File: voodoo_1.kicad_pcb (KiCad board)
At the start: 2 copper layers, 70 x 50 mm, 37 parts, among them Q1 2N2222, Q2 2N2222, U1 LM308

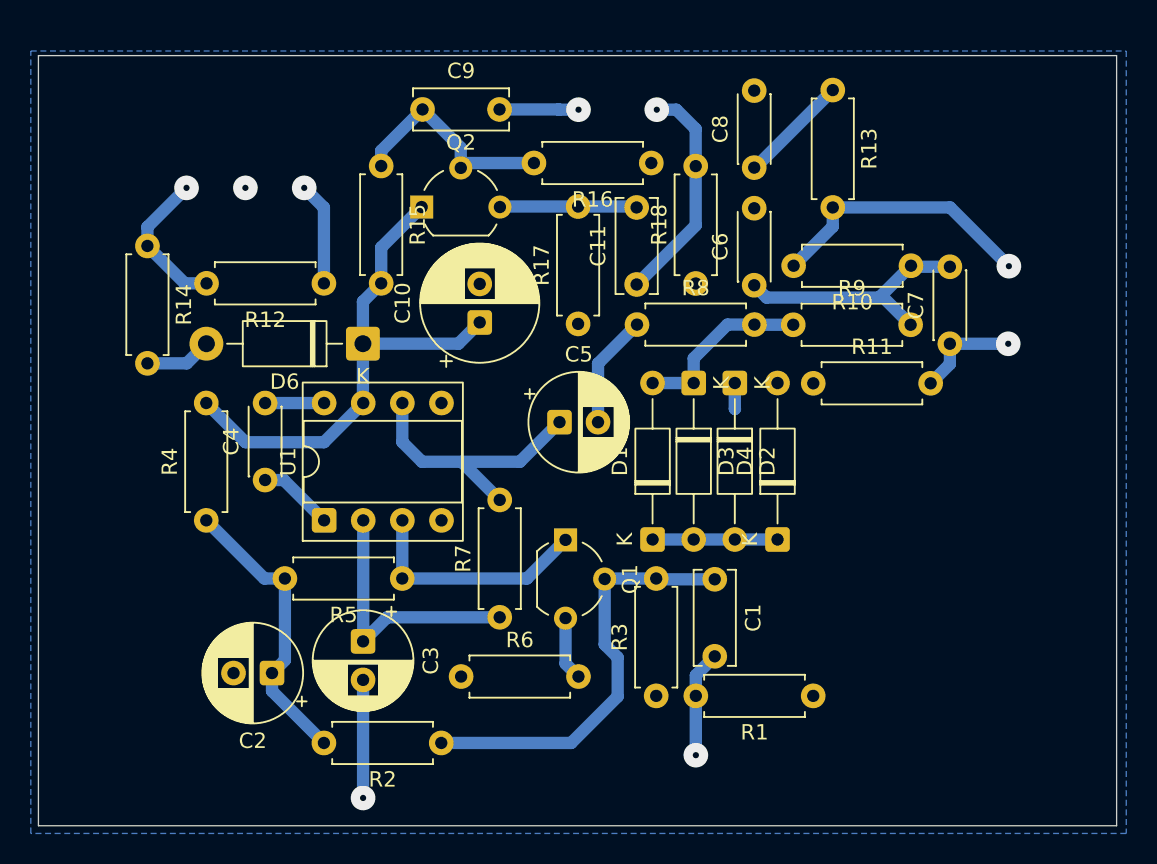
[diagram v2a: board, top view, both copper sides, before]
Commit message: 上下幅を修正
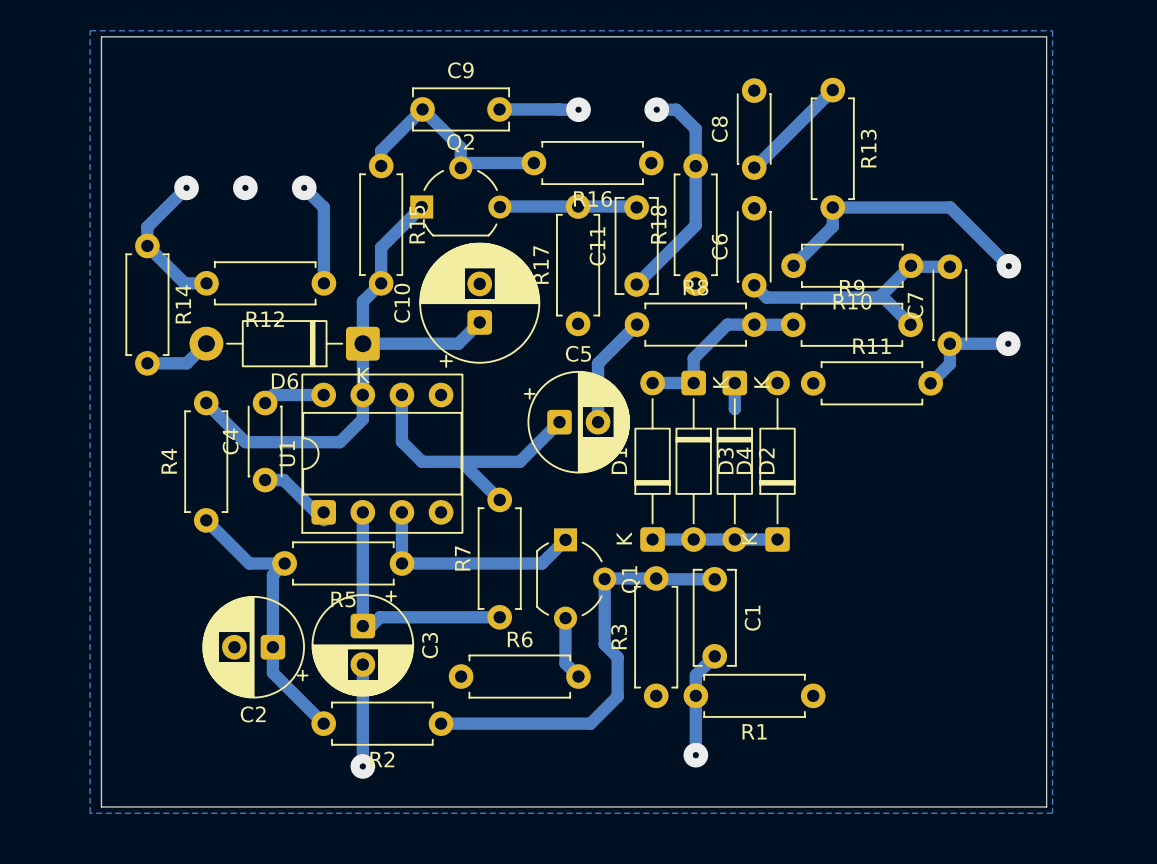
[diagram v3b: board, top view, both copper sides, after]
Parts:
- moved C2 1.68 mm to (113.5, 103.5)
- moved R2 1.25 mm to (124.4, 108.4)
- moved C3 1.00 mm to (119.3, 102.1)
- moved R5 0.98 mm to (121.9, 98.0)
- moved U1 0.52 mm to (116.8, 94.7)
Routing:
- net Net-(C3-Pad2): track 7.69 -> 6.61 mm
- net Net-(U1--): track 17.4 -> 16.5 mm
- net Net-(Q1-C): track 15.5 -> 14.7 mm
- net Net-(C2-Pad1): track 19.1 -> 18.3 mm
- net Net-(D6-K): track 34.8 -> 35.4 mm
- net Net-(C5-Pad1): track 17.8 -> 18.4 mm
- net Net-(Q1-B): track 27.9 -> 27.4 mm
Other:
- board size 70 x 50 mm -> 61.4 x 50 mm
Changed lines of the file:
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@@
 	(footprint "Resistor_THT:R_Axial_DIN0207_L6.3mm_D2.5mm_P7.62mm_Horizontal"
 		(layer "F.Cu")
-		(at 124.439065 109.694505 180)
+		(at 124.424791 108.440272 180)
 		(descr "Resistor, Axial_DIN0207 series, Axial, Horizontal, pin pitch=7.62mm, 0.25W = 1/4W, length*diameter=6.3*2.5mm^2, http://cdn-reichelt.de/documents/datenblatt/B400/1_4W%23YAG.pdf")
 		(tags "Resistor Axial_DIN0207 series Axial Horizontal pin pitch 7.62mm 0.25W = 1/4W length 6.3mm diameter 2.5mm")
@@
 	(footprint "Capacitor_THT:CP_Radial_D6.3mm_P2.50mm"
 		(layer "F.Cu")
-		(at 113.45038 105.156 180)
+		(at 113.508973 103.477911 180)
 		(descr "CP, Radial series, Radial, pin pitch=2.50mm, diameter=6.3mm, height=7mm, Electrolytic Capacitor")
 		(tags "CP Radial series Radial pin pitch 2.50mm diameter 6.3mm height 7mm Electrolytic Capacitor")
@@
 	(footprint "Package_DIP:DIP-8_W7.62mm_Socket"
 		(layer "F.Cu")
-		(at 116.833021 95.243021 90)
+		(at 116.804791 94.723635 90)
 		(descr "8-lead though-hole mounted DIP package, row spacing 7.62mm (300 mils), Socket")
 		(tags "THT DIP DIL PDIP 2.54mm 7.62mm 300mil Socket")
@@
 	(footprint "Resistor_THT:R_Axial_DIN0207_L6.3mm_D2.5mm_P7.62mm_Horizontal"
 		(layer "F.Cu")
-		(at 121.906043 99.018131 180)
+		(at 121.89082 98.04043 180)
 		(descr "Resistor, Axial_DIN0207 series, Axial, Horizontal, pin pitch=7.62mm, 0.25W = 1/4W, length*diameter=6.3*2.5mm^2, http://cdn-reichelt.de/documents/datenblatt/B400/1_4W%23YAG.pdf")
 		(tags "Resistor Axial_DIN0207 series Axial Horizontal pin pitch 7.62mm 0.25W = 1/4W length 6.3mm diameter 2.5mm")
@@
 	(footprint "Capacitor_THT:CP_Radial_D6.3mm_P2.50mm"
 		(layer "F.Cu")
-		(at 119.362554 103.100274 -90)
+		(at 119.347806 102.105343 -90)
 		(descr "CP, Radial series, Radial, pin pitch=2.50mm, diameter=6.3mm, height=7mm, Electrolytic Capacitor")
 		(tags "CP Radial series Radial pin pitch 2.50mm diameter 6.3mm height 7mm Electrolytic Capacitor")
@@
 	)
 	(gr_rect
-		(start 98.28465 65.068978)
-		(end 168.28465 115.068978)
+		(start 102.377468 63.851135)
+		(end 163.741468 113.851135)
 		(stroke
 			(width 0.05)
@@
 	)
 	(segment
-		(start 124.439065 109.694505)
-		(end 132.875495 109.694505)
-		(width 0.8)
-		(layer "B.Cu")
-		(net 2)
-	)
-	(segment
 		(start 135.047487 103.297487)
 		(end 135.89 104.14)
@@
 	)
 	(segment
-		(start 132.875495 109.694505)
-		(end 135.89 106.68)
+		(start 138.393158 99.017213)
+		(end 135.080771 99.017213)
 		(width 0.8)
 		(layer "B.Cu")
@@
 	)
 	(segment
-		(start 138.393158 99.017213)
-		(end 135.080771 99.017213)
+		(start 142.19424 99.069103)
+		(end 138.445048 99.069103)
 		(width 0.8)
 		(layer "B.Cu")
@@
 	)
 	(segment
-		(start 142.19424 99.069103)
-		(end 138.445048 99.069103)
+		(start 124.424791 108.440272)
+		(end 134.129728 108.440272)
 		(width 0.8)
 		(layer "B.Cu")
@@
 	)
 	(segment
+		(start 134.129728 108.440272)
+		(end 135.89 106.68)
+		(width 0.8)
+		(layer "B.Cu")
+		(net 2)
+	)
+	(segment
 		(start 135.89 104.14)
 		(end 135.89 106.68)
@@
 	)
 	(segment
-		(start 112.95673 99.018131)
+		(start 111.979029 98.04043)
 		(end 109.18162 95.243021)
 		(width 0.8)
@@
 	)
 	(segment
-		(start 114.286043 99.018131)
-		(end 114.286043 104.320337)
+		(start 114.27082 98.04043)
+		(end 111.979029 98.04043)
 		(width 0.8)
 		(layer "B.Cu")
@@
 	)
 	(segment
-		(start 114.286043 99.018131)
-		(end 112.95673 99.018131)
+		(start 113.508973 103.477911)
+		(end 113.508973 105.144454)
 		(width 0.8)
 		(layer "B.Cu")
@@
 	)
 	(segment
-		(start 114.286043 104.320337)
-		(end 113.45038 105.156)
+		(start 113.508973 98.802277)
+		(end 114.27082 98.04043)
 		(width 0.8)
 		(layer "B.Cu")
@@
 	)
 	(segment
-		(start 113.45038 105.156)
-		(end 113.45038 106.32582)
+		(start 113.508973 105.144454)
+		(end 116.804791 108.440272)
 		(width 0.8)
 		(layer "B.Cu")
@@
 	)
 	(segment
-		(start 113.45038 106.32582)
-		(end 116.819065 109.694505)
+		(start 113.508973 103.477911)
+		(end 113.508973 98.802277)
 		(width 0.8)
 		(layer "B.Cu")
@@
 	)
 	(via
-		(at 119.362554 113.266554)
+		(at 119.347806 111.219806)
 		(size 1.6)
 		(drill 0.4)
@@
 	)
 	(segment
-		(start 119.362554 113.266554)
-		(end 119.38 113.284)
+		(start 119.347806 104.605343)
+		(end 119.347806 111.219806)
 		(width 0.8)
 		(layer "B.Cu")
@@
 	)
 	(segment
-		(start 119.362554 105.600274)
-		(end 119.362554 113.266554)
+		(start 120.46018 101.53582)
+		(end 128.233743 101.53582)
 		(width 0.8)
 		(layer "B.Cu")
-		(net 5)
+		(net 7)
 	)
 	(segment
-		(start 119.373021 95.243021)
-		(end 119.373021 103.089807)
+		(start 119.344791 94.723635)
+		(end 119.344791 102.102328)
 		(width 0.8)
 		(layer "B.Cu")
@@
 	)
 	(segment
-		(start 120.927008 101.53582)
-		(end 119.362554 103.100274)
+		(start 119.344791 102.102328)
+		(end 119.347806 102.105343)
 		(width 0.8)
 		(layer "B.Cu")
@@
 	)
 	(segment
-		(start 128.233743 101.53582)
-		(end 120.927008 101.53582)
+		(start 119.347806 102.105343)
+		(end 119.890657 102.105343)
 		(width 0.8)
 		(layer "B.Cu")
@@
 	)
 	(segment
-		(start 119.373021 103.089807)
-		(end 119.362554 103.100274)
+		(start 119.890657 102.105343)
+		(end 120.46018 101.53582)
 		(width 0.8)
 		(layer "B.Cu")
@@
 	)
 	(segment
-		(start 116.8314 87.624642)
-		(end 116.833021 87.623021)
+		(start 116.804791 87.103635)
+		(end 113.523094 87.103635)
 		(width 0.8)
 		(layer "B.Cu")
@@
 	)
 	(segment
-		(start 113.002087 87.624642)
-		(end 116.8314 87.624642)
+		(start 113.523094 87.103635)
+		(end 113.002087 87.624642)
 		(width 0.8)
 		(layer "B.Cu")
@@
 	)
 	(segment
-		(start 119.373021 87.623021)
-		(end 116.826042 90.17)
+		(start 119.352076 83.77307)
+		(end 119.352076 87.09635)
 		(width 0.8)
 		(layer "B.Cu")
@@
 	)
 	(segment
-		(start 109.18162 87.623021)
-		(end 111.728599 90.17)
+		(start 119.352076 81.040531)
+		(end 120.538306 79.854301)
 		(width 0.8)
 		(layer "B.Cu")
@@
 	)
 	(segment
-		(start 119.352076 81.040531)
-		(end 120.538306 79.854301)
+		(start 120.538306 79.854301)
+		(end 120.538306 77.528397)
 		(width 0.8)
 		(layer "B.Cu")
@@
 	)
 	(segment
-		(start 120.538306 79.854301)
-		(end 120.538306 77.528397)
+		(start 111.728599 90.17)
+		(end 109.18162 87.623021)
+		(width 0.8)
+		(layer "B.Cu")
+		(net 17)
+	)
+	(segment
+		(start 119.352076 87.09635)
+		(end 119.344791 87.103635)
 		(width 0.8)
 		(layer "B.Cu")
@@
 	)
 	(segment
-		(start 119.352076 83.77307)
-		(end 119.352076 81.040531)
+		(start 119.344791 88.681209)
+		(end 117.856 90.17)
 		(width 0.8)
 		(layer "B.Cu")
@@
 	)
 	(segment
-		(start 119.352076 83.77307)
-		(end 119.352076 87.602076)
+		(start 117.856 90.17)
+		(end 111.728599 90.17)
 		(width 0.8)
 		(layer "B.Cu")
@@
 	)
 	(segment
-		(start 116.826042 90.17)
-		(end 111.728599 90.17)
+		(start 119.352076 83.77307)
+		(end 119.352076 81.040531)
 		(width 0.8)
 		(layer "B.Cu")
@@
 	)
 	(segment
-		(start 125.553892 83.77307)
-		(end 126.935235 82.391727)
+		(start 119.344791 87.103635)
+		(end 119.344791 88.681209)
 		(width 0.8)
 		(layer "B.Cu")
@@
 	)
 	(segment
-		(start 119.352076 87.602076)
-		(end 119.373021 87.623021)
+		(start 125.553892 83.77307)
+		(end 126.935235 82.391727)
 		(width 0.8)
 		(layer "B.Cu")
@@
 	)
 	(segment
-		(start 121.913021 95.243021)
-		(end 121.913021 99.011153)
+		(start 130.977554 98.04043)
+		(end 132.507487 96.510497)
 		(width 0.8)
 		(layer "B.Cu")
@@
 	)
 	(segment
-		(start 132.507487 96.510497)
-		(end 132.507487 96.600513)
+		(start 121.884791 94.723635)
+		(end 121.884791 98.034401)
 		(width 0.8)
 		(layer "B.Cu")
@@
 	)
 	(segment
-		(start 121.913021 99.011153)
-		(end 121.906043 99.018131)
+		(start 132.507487 96.510497)
+		(end 132.507487 96.600513)
 		(width 0.8)
 		(layer "B.Cu")
@@
 	)
 	(segment
-		(start 129.999853 99.018131)
-		(end 132.507487 96.510497)
+		(start 121.884791 98.034401)
+		(end 121.89082 98.04043)
 		(width 0.8)
 		(layer "B.Cu")
@@
 	)
 	(segment
-		(start 121.906043 99.018131)
-		(end 129.999853 99.018131)
+		(start 121.89082 98.04043)
+		(end 130.977554 98.04043)
 		(width 0.8)
 		(layer "B.Cu")
@@
 	)
 	(segment
-		(start 123.19 91.44)
-		(end 121.913021 90.163021)
+		(start 129.54 91.44)
+		(end 125.757923 91.44)
 		(width 0.8)
 		(layer "B.Cu")
@@
 	)
 	(segment
-		(start 129.54 91.44)
-		(end 125.757923 91.44)
+		(start 132.111402 88.868598)
+		(end 129.54 91.44)
 		(width 0.8)
 		(layer "B.Cu")
@@
 	)
 	(segment
-		(start 132.111402 88.868598)
-		(end 129.54 91.44)
+		(start 125.757923 91.44)
+		(end 123.19 91.44)
 		(width 0.8)
 		(layer "B.Cu")
@@
 	)
 	(segment
-		(start 121.913021 90.163021)
-		(end 121.913021 87.623021)
+		(start 121.884791 90.134791)
+		(end 121.884791 87.103635)
 		(width 0.8)
 		(layer "B.Cu")
@@
 	)
 	(segment
-		(start 125.757923 91.44)
-		(end 123.19 91.44)
+		(start 123.19 91.44)
+		(end 121.884791 90.134791)
 		(width 0.8)
 		(layer "B.Cu")
@@
 		(min_thickness 0.25)
 		(filled_areas_thickness no)
-		(fill yes
+		(fill
 			(mode hatch)
 			(thermal_gap 0.5)
@@
 		(polygon
 			(pts
-				(xy 97.79 64.77) (xy 168.91 64.77) (xy 168.91 115.57) (xy 97.79 115.57)
+				(xy 101.642835 63.458628) (xy 164.126835 63.458628) (xy 164.126835 114.258628) (xy 101.642835 114.258628)
 			)
 		)

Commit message: 4番ピンがGNDに接続されてなかった
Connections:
- U1 pad 4: unconnected-(U1-V--Pad4) -> GND

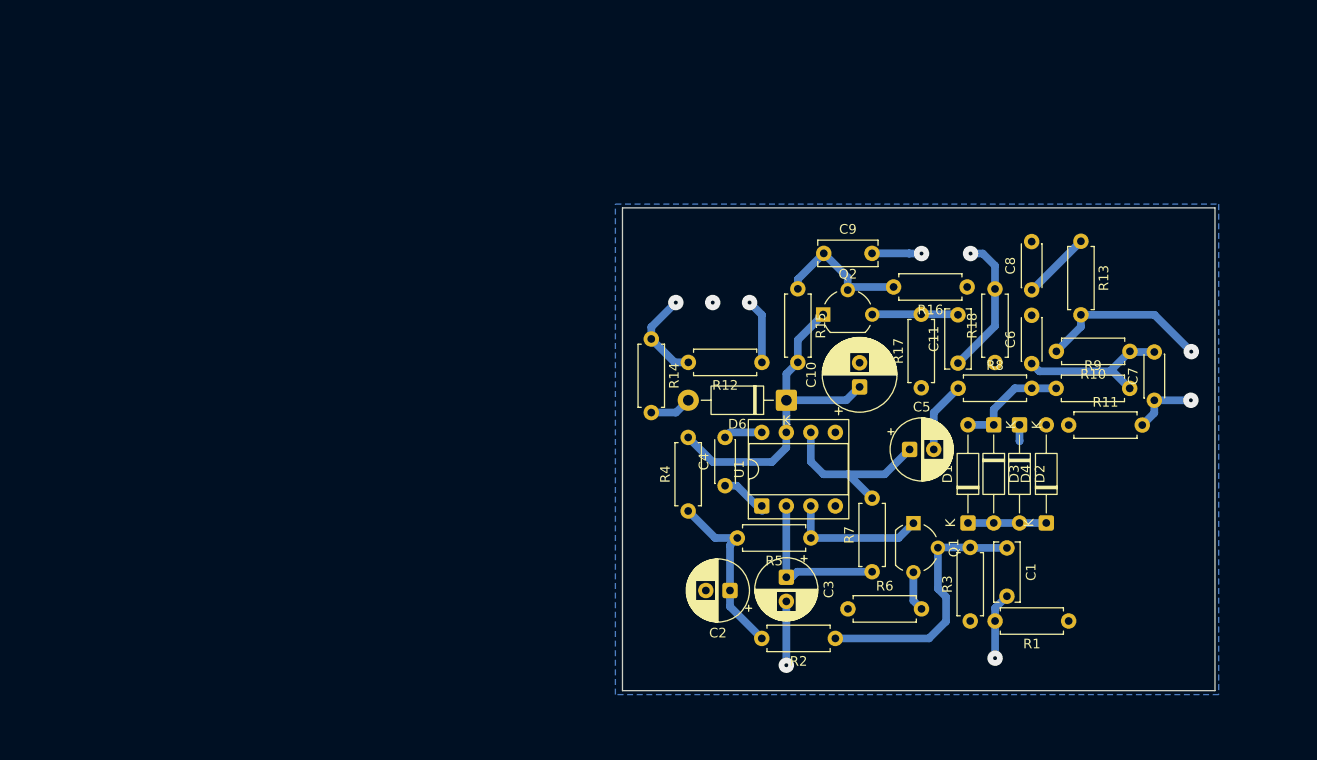
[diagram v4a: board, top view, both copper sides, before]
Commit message: GNDを1.0mmに、ドリル穴を0.4mmに、部品の配置をやり直し。
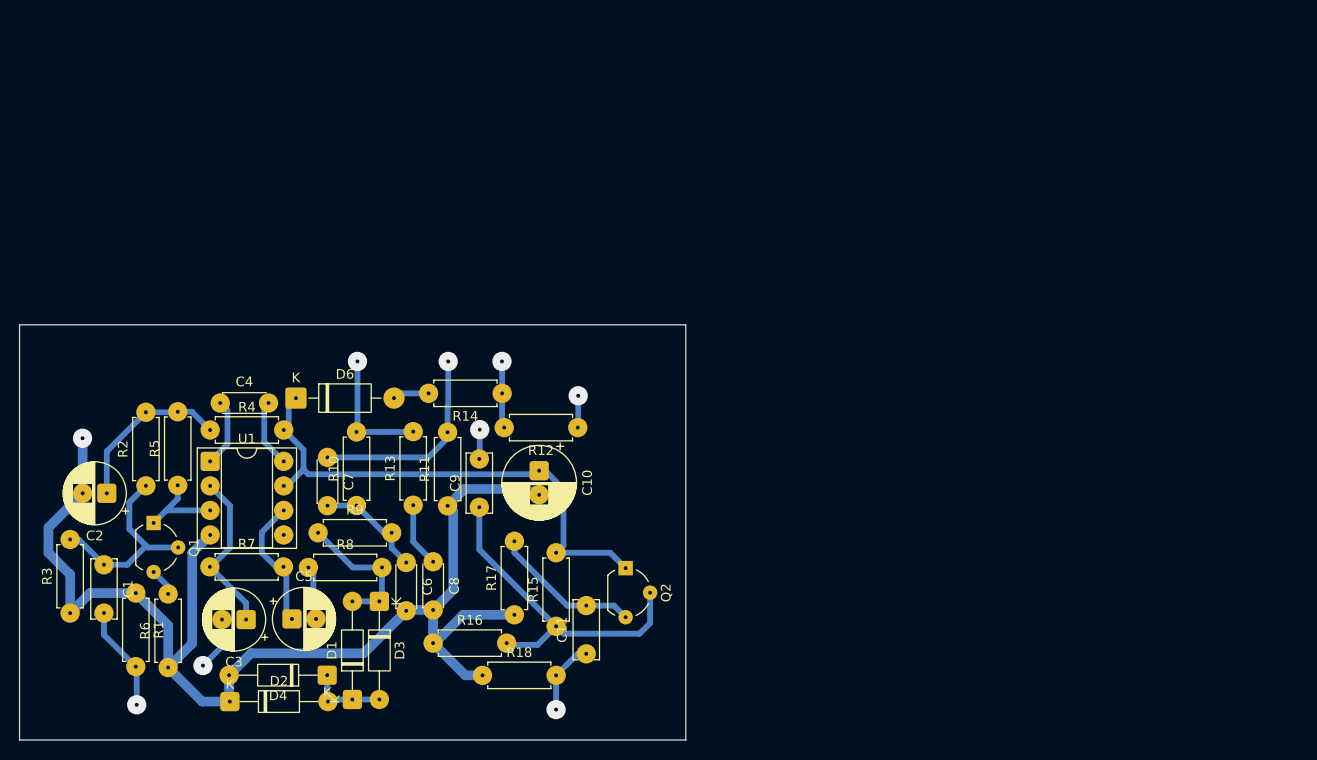
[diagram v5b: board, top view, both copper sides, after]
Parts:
- moved R1 96.7 mm to (52.0, 103.7), turned to -90 degrees
- moved C1 93.5 mm to (48.7, 100.8)
- moved R3 93.2 mm to (45.2, 105.8)
- moved D2 86.7 mm to (61.7, 115.0), turned to 0 degrees
- moved C7 85.8 mm to (71.8, 89.7), turned to -90 degrees
- moved R10 81.7 mm to (74.8, 94.7), turned to 90 degrees
- moved Q1 78.7 mm to (53.8, 96.5)
- moved R9 77.9 mm to (70.9, 97.5)
- moved D4 76.1 mm to (71.8, 112.2), turned to 180 degrees
- moved R13 74.4 mm to (80.7, 94.6), turned to 90 degrees
- moved R2 73.1 mm to (53.0, 92.6), turned to 90 degrees
- moved R6 70.7 mm to (55.3, 111.5), turned to 90 degrees
- moved R8 69.8 mm to (69.8, 101.1)
- moved R7 68.6 mm to (59.6, 101.0), turned to 0 degrees
- moved C8 68.1 mm to (82.8, 100.5), turned to -90 degrees
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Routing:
- net GND: track 1.69 -> 130.1 mm
- net Net-(Q2-B): track 14.7 -> 35.2 mm
- net Net-(D6-K): track 35.4 -> 54.4 mm
- net Net-(C7-Pad1): track 6.87 -> 21.2 mm
- net Net-(SW1B-C): track 14.7 -> 7.85 mm
- net Net-(Q1-B): track 27.4 -> 20.8 mm
- net Net-(Q2-E): track 8.95 -> 15.5 mm
- net Net-(Q1-C): track 14.7 -> 9.48 mm
- net Net-(C6-Pad1): track 16.7 -> 11.5 mm
- net Net-(R10-Pad2): track 17.8 -> 13.2 mm
- net Net-(C5-Pad1): track 18.4 -> 13.9 mm
- net Net-(SW1A-C): track 6.93 -> 10.4 mm
- net Net-(SW1C-C): track 6.73 -> 3.30 mm
- net Net-(U1-COMP2): track 4.02 -> 7.06 mm
- net Net-(D1-A): track 11.7 -> 14.5 mm
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- removed copper zone on B.Cu, net GND
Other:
- board size 61.4 x 50 mm -> 69 x 43 mm
